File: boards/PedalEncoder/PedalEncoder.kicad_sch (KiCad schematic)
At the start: 35 parts, among them J1 Pwr, J2 Control, J3 Switch, J4 ISP, J5 Pedal, J6 MIDI Out, J7 I2C, Q1 BC547, Q2 BC547, U1 4069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

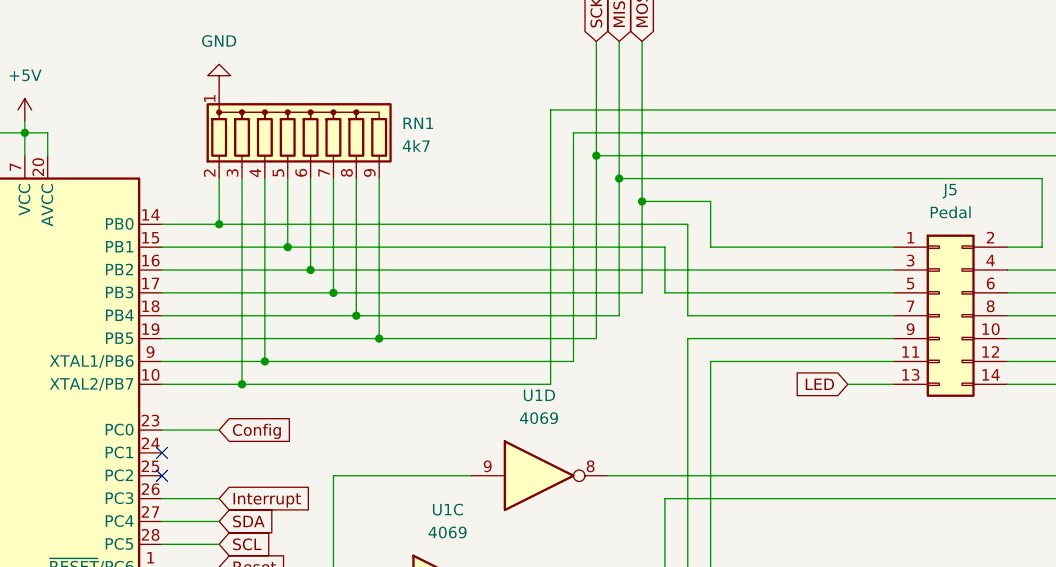
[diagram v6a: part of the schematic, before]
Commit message: Fixed PedalEncoder ISP connections
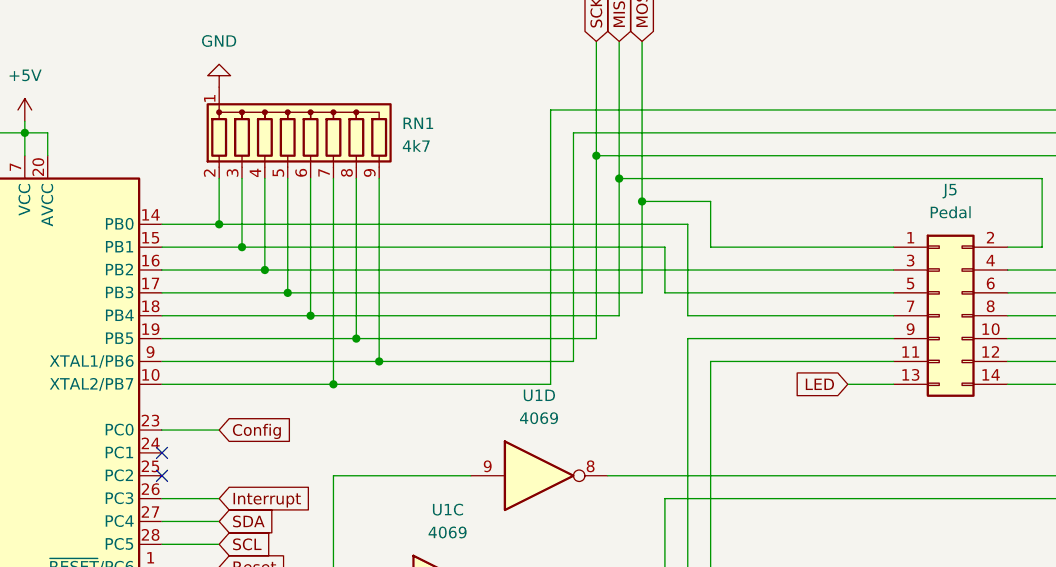
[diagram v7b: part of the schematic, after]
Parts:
- Q1, Q2: footprint Package_TO_SOT_THT:TO-92_Inline_Wide -> Package_TO_SOT_THT:TO-92L_Inline
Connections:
- net MISO: now also RN1.6 (R5); no longer RN1.8 (R7)
- net MOSI: now also RN1.5 (R4); no longer RN1.7 (R6)
- net SCK: now also RN1.8 (R7); no longer RN1.9 (R8)
- net at J5.8 (Pin_8), U2.10 (XTAL2/PB7): now also RN1.7 (R6); no longer RN1.3 (R2)
- net at J5.6 (Pin_6), U2.9 (XTAL1/PB6): now also RN1.9 (R8); no longer RN1.4 (R3)
- net at J5.5 (Pin_5), U2.15 (PB1): now also RN1.3 (R2); no longer RN1.5 (R4)
- net at J5.3 (Pin_3), U2.16 (PB2): now also RN1.4 (R3); no longer RN1.6 (R5)
